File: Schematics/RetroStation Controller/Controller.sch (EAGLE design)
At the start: 10 parts, among them U2 JOYSTICKPTH

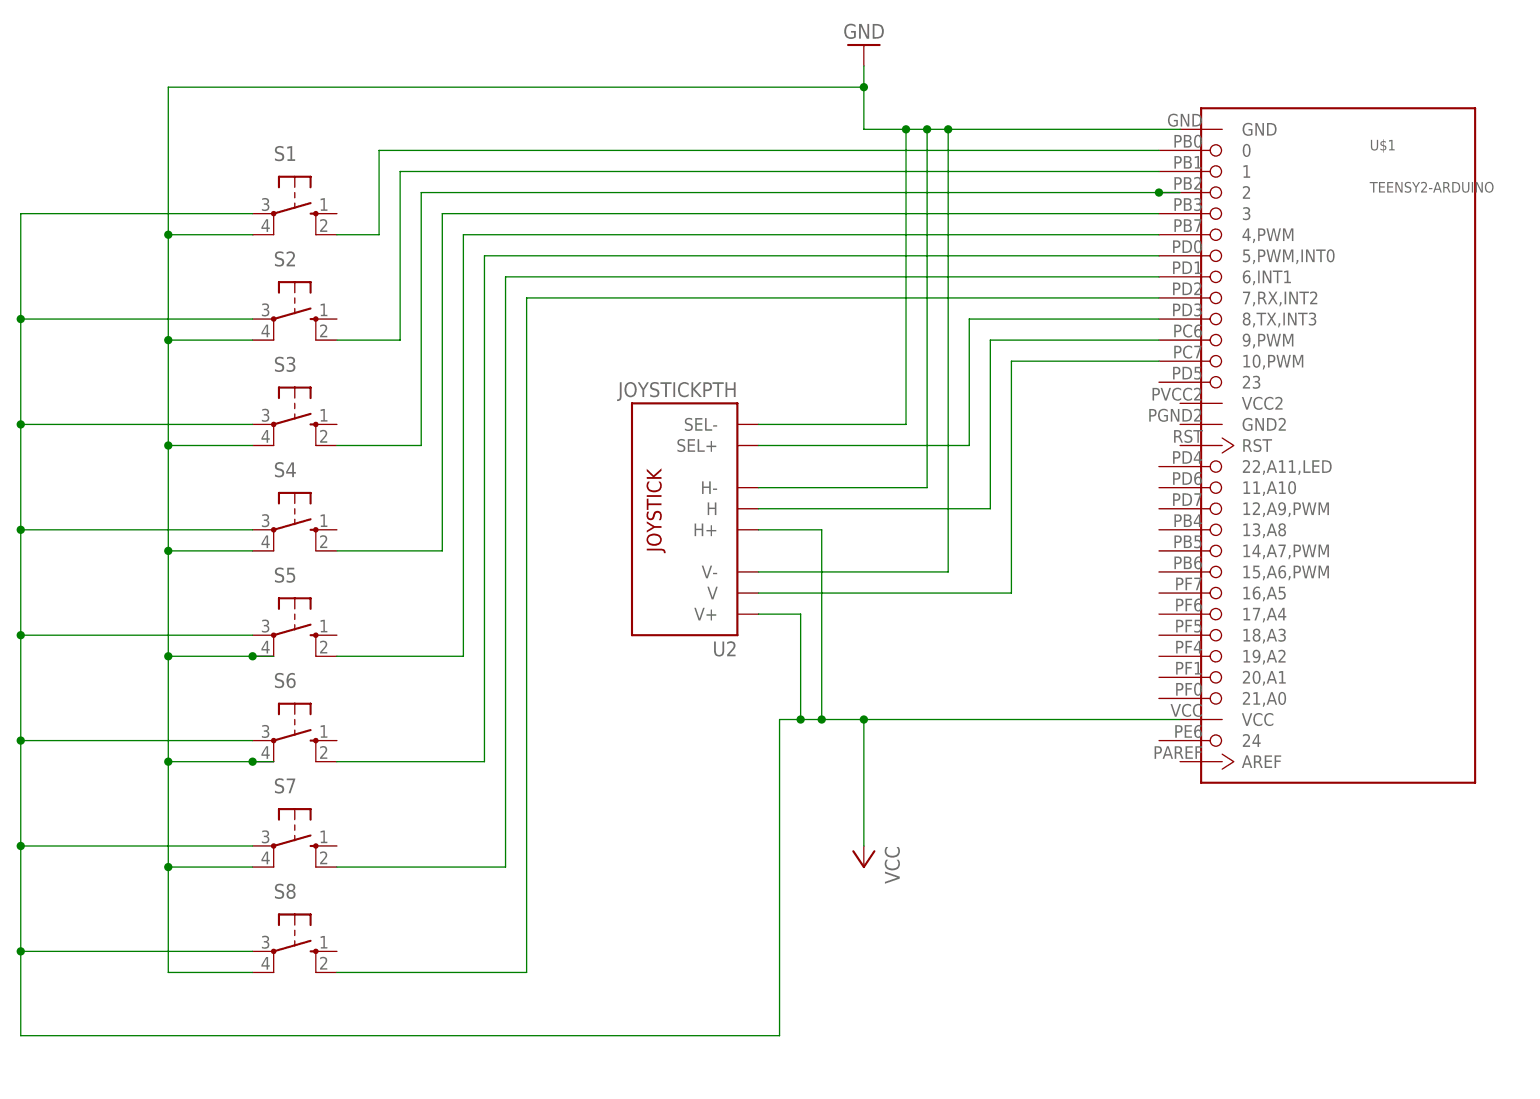
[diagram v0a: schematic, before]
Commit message: Schematics updated to reflect the use of the internal pull-up resistors of the controller's microcontroller Firmware for the internal controller's microcontroller started
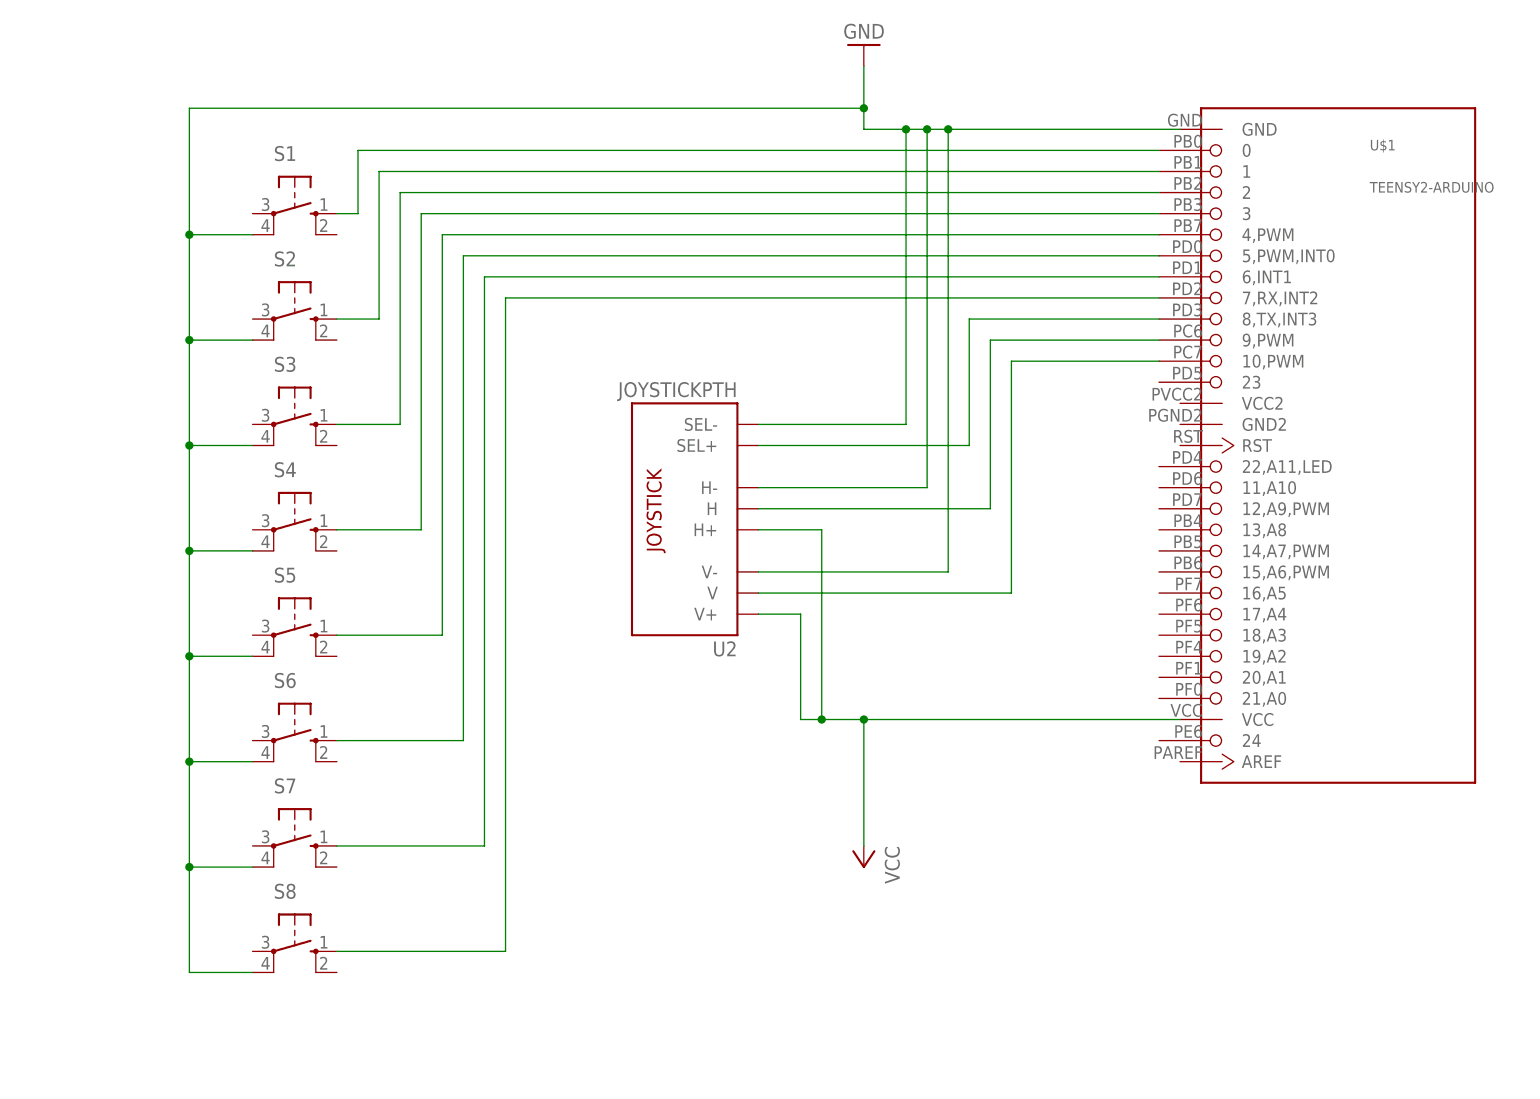
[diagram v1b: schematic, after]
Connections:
- net N$1: now also S1.S; no longer S1.S1
- net N$2: now also S2.S; no longer S2.S1
- net N$3: now also S3.S; no longer S3.S1
- net N$4: now also S4.S; no longer S4.S1
- net N$5: now also S5.S; no longer S5.S1
- net N$6: now also S6.S; no longer S6.S1
- net N$7: now also S7.S; no longer S7.S1
- net N$8: now also S8.S; no longer S8.S1
- net VCC: no longer S1.P, S2.P, S3.P, S4.P, S5.P, S6.P, S7.P, S8.P

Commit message: Created seperate circuits for each button panel.
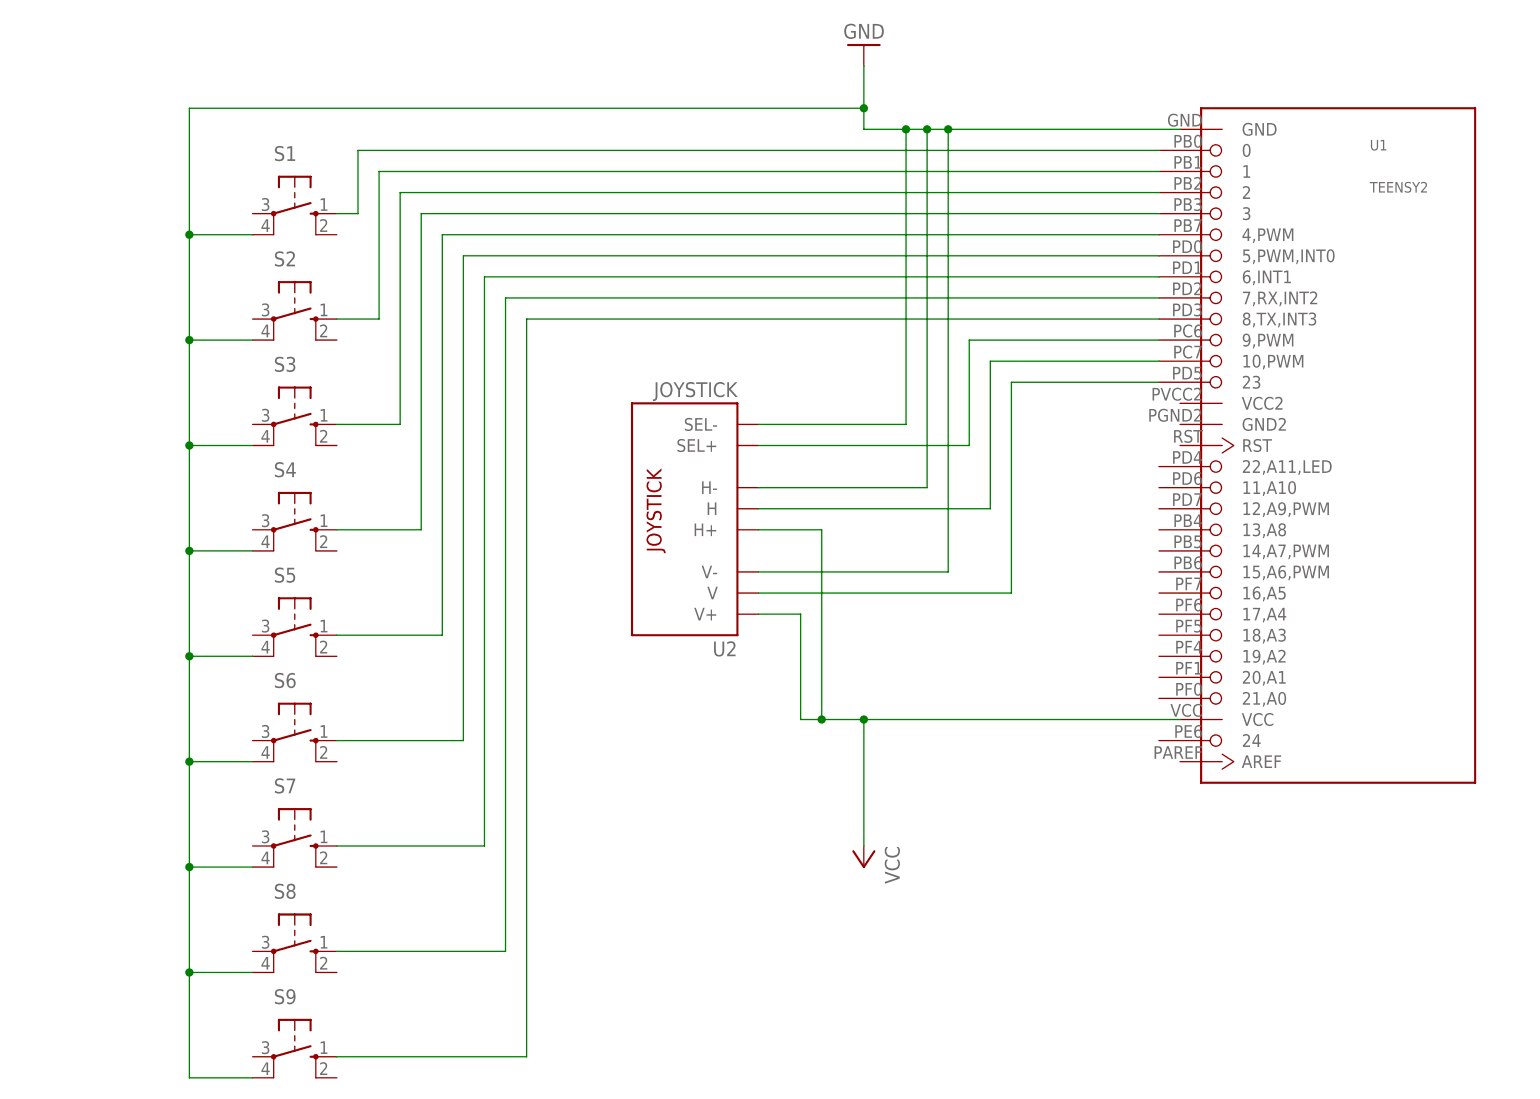
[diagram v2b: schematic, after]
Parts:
- added S9: (no value), switch-omron:10-XX
- U1: value TEENSY2-ARDUINO -> TEENSY2
- U2: value JOYSTICKPTH -> JOYSTICK
- renumbered U$1 to U1
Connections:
- removed net N$13: U1.10,PWM, U2.V
- new net N$10: U1.10,PWM, U2.H
- new net N$9: U1.23, U2.V
- net GND: now also S9.P1
- net N$11: now also U1.9,PWM; no longer U1.8,TX,INT3
- net N$12: now also S9.S, U1.8,TX,INT3; no longer U1.9,PWM, U2.H
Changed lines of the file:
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@@
 </classes>
 <parts>
-<part name="U$1" library="teensy2" deviceset="TEENSY2-ARDUINO" device=""/>
+<part name="U1" library="teensy2" deviceset="TEENSY2-ARDUINO" device="" value="TEENSY2"/>
 <part name="P+1" library="supply1" deviceset="VCC" device=""/>
 <part name="GND" library="supply1" deviceset="GND" device=""/>
@@
 <part name="S7" library="switch-omron" deviceset="10-XX" device=""/>
 <part name="S8" library="switch-omron" deviceset="10-XX" device=""/>
-<part name="U2" library="SparkFun-Electromechanical" deviceset="JOYSTICK" device="PTH"/>
+<part name="U2" library="SparkFun-Electromechanical" deviceset="JOYSTICK" device="PTH" value="JOYSTICK"/>
 <part name="FRAME1" library="frames" deviceset="LETTER_L" device=""/>
+<part name="S9" library="switch-omron" deviceset="10-XX" device=""/>
 </parts>
 <sheets>
@@
 </plain>
 <instances>
-<instance part="U$1" gate="G$1" x="198.12" y="109.22"/>
+<instance part="U1" gate="G$1" x="198.12" y="109.22"/>
 <instance part="P+1" gate="VCC" x="137.16" y="55.88" rot="R180"/>
 <instance part="GND" gate="1" x="137.16" y="154.94" rot="R180"/>
@@
 <instance part="FRAME1" gate="G$1" x="0" y="0"/>
 <instance part="FRAME1" gate="G$2" x="147.32" y="0"/>
+<instance part="S9" gate="1" x="68.58" y="33.02" rot="R270"/>
 </instances>
 <busses>
@@
 <pinref part="P+1" gate="VCC" pin="VCC"/>
 <wire x1="137.16" y1="58.42" x2="137.16" y2="73.66" width="0.1524" layer="91"/>
-<pinref part="U$1" gate="G$1" pin="VCC"/>
+<pinref part="U1" gate="G$1" pin="VCC"/>
 <wire x1="137.16" y1="73.66" x2="175.26" y2="73.66" width="0.1524" layer="91"/>
 <junction x="137.16" y="73.66"/>
@@
 <net name="GND" class="0">
 <segment>
-<pinref part="U$1" gate="G$1" pin="GND"/>
+<pinref part="U1" gate="G$1" pin="GND"/>
 <pinref part="GND" gate="1" pin="GND"/>
 <wire x1="137.16" y1="152.4" x2="137.16" y2="147.32" width="0.1524" layer="91"/>
@@
 <wire x1="55.88" y1="43.18" x2="55.88" y2="55.88" width="0.1524" layer="91"/>
 <junction x="55.88" y="55.88"/>
-</segment>
-</net>
-<net name="N$11" class="0">
-<segment>
-<pinref part="U2" gate="G$1" pin="SEL+"/>
-<wire x1="124.46" y1="106.68" x2="149.86" y2="106.68" width="0.1524" layer="91"/>
-<wire x1="149.86" y1="106.68" x2="149.86" y2="121.92" width="0.1524" layer="91"/>
-<pinref part="U$1" gate="G$1" pin="8,TX,INT3"/>
-<wire x1="149.86" y1="121.92" x2="172.72" y2="121.92" width="0.1524" layer="91"/>
-</segment>
-</net>
-<net name="N$12" class="0">
-<segment>
-<pinref part="U2" gate="G$1" pin="H"/>
-<wire x1="124.46" y1="99.06" x2="152.4" y2="99.06" width="0.1524" layer="91"/>
-<wire x1="152.4" y1="99.06" x2="152.4" y2="119.38" width="0.1524" layer="91"/>
-<pinref part="U$1" gate="G$1" pin="9,PWM"/>
-<wire x1="152.4" y1="119.38" x2="172.72" y2="119.38" width="0.1524" layer="91"/>
-</segment>
-</net>
-<net name="N$13" class="0">
-<segment>
-<pinref part="U2" gate="G$1" pin="V"/>
-<wire x1="124.46" y1="88.9" x2="154.94" y2="88.9" width="0.1524" layer="91"/>
-<wire x1="154.94" y1="88.9" x2="154.94" y2="116.84" width="0.1524" layer="91"/>
-<pinref part="U$1" gate="G$1" pin="10,PWM"/>
-<wire x1="154.94" y1="116.84" x2="172.72" y2="116.84" width="0.1524" layer="91"/>
+<pinref part="S9" gate="1" pin="P1"/>
+<wire x1="63.5" y1="30.48" x2="55.88" y2="30.48" width="0.1524" layer="91"/>
+<wire x1="55.88" y1="30.48" x2="55.88" y2="43.18" width="0.1524" layer="91"/>
+<junction x="55.88" y="43.18"/>
 </segment>
 </net>
@@
 <wire x1="73.66" y1="134.62" x2="76.2" y2="134.62" width="0.1524" layer="91"/>
 <wire x1="76.2" y1="134.62" x2="76.2" y2="142.24" width="0.1524" layer="91"/>
-<pinref part="U$1" gate="G$1" pin="0"/>
+<pinref part="U1" gate="G$1" pin="0"/>
 <wire x1="76.2" y1="142.24" x2="172.72" y2="142.24" width="0.1524" layer="91"/>
 </segment>
@@
 <wire x1="73.66" y1="121.92" x2="78.74" y2="121.92" width="0.1524" layer="91"/>
 <wire x1="78.74" y1="121.92" x2="78.74" y2="139.7" width="0.1524" layer="91"/>
-<pinref part="U$1" gate="G$1" pin="1"/>
+<pinref part="U1" gate="G$1" pin="1"/>
 <wire x1="78.74" y1="139.7" x2="172.72" y2="139.7" width="0.1524" layer="91"/>
 </segment>
@@
 <wire x1="73.66" y1="109.22" x2="81.28" y2="109.22" width="0.1524" layer="91"/>
 <wire x1="81.28" y1="109.22" x2="81.28" y2="137.16" width="0.1524" layer="91"/>
-<pinref part="U$1" gate="G$1" pin="2"/>
+<pinref part="U1" gate="G$1" pin="2"/>
 <wire x1="81.28" y1="137.16" x2="172.72" y2="137.16" width="0.1524" layer="91"/>
 </segment>
@@
 <wire x1="73.66" y1="96.52" x2="83.82" y2="96.52" width="0.1524" layer="91"/>
 <wire x1="83.82" y1="96.52" x2="83.82" y2="134.62" width="0.1524" layer="91"/>
-<pinref part="U$1" gate="G$1" pin="3"/>
+<pinref part="U1" gate="G$1" pin="3"/>
 <wire x1="83.82" y1="134.62" x2="172.72" y2="134.62" width="0.1524" layer="91"/>
 </segment>
@@
 <wire x1="73.66" y1="83.82" x2="86.36" y2="83.82" width="0.1524" layer="91"/>
 <wire x1="86.36" y1="83.82" x2="86.36" y2="132.08" width="0.1524" layer="91"/>
-<pinref part="U$1" gate="G$1" pin="4,PWM"/>
+<pinref part="U1" gate="G$1" pin="4,PWM"/>
 <wire x1="86.36" y1="132.08" x2="172.72" y2="132.08" width="0.1524" layer="91"/>
 </segment>
@@
 <wire x1="73.66" y1="71.12" x2="88.9" y2="71.12" width="0.1524" layer="91"/>
 <wire x1="88.9" y1="71.12" x2="88.9" y2="129.54" width="0.1524" layer="91"/>
-<pinref part="U$1" gate="G$1" pin="5,PWM,INT0"/>
+<pinref part="U1" gate="G$1" pin="5,PWM,INT0"/>
 <wire x1="88.9" y1="129.54" x2="172.72" y2="129.54" width="0.1524" layer="91"/>
 </segment>
@@
 <wire x1="73.66" y1="58.42" x2="91.44" y2="58.42" width="0.1524" layer="91"/>
 <wire x1="91.44" y1="58.42" x2="91.44" y2="127" width="0.1524" layer="91"/>
-<pinref part="U$1" gate="G$1" pin="6,INT1"/>
+<pinref part="U1" gate="G$1" pin="6,INT1"/>
 <wire x1="91.44" y1="127" x2="172.72" y2="127" width="0.1524" layer="91"/>
 </segment>
@@
 <wire x1="73.66" y1="45.72" x2="93.98" y2="45.72" width="0.1524" layer="91"/>
 <wire x1="93.98" y1="45.72" x2="93.98" y2="124.46" width="0.1524" layer="91"/>
-<pinref part="U$1" gate="G$1" pin="7,RX,INT2"/>
+<pinref part="U1" gate="G$1" pin="7,RX,INT2"/>
 <wire x1="93.98" y1="124.46" x2="172.72" y2="124.46" width="0.1524" layer="91"/>
 </segment>
 </net>
+<net name="N$9" class="0">
+<segment>
+<pinref part="U2" gate="G$1" pin="V"/>
+<wire x1="124.46" y1="88.9" x2="154.94" y2="88.9" width="0.1524" layer="91"/>
+<wire x1="154.94" y1="88.9" x2="154.94" y2="114.3" width="0.1524" layer="91"/>
+<pinref part="U1" gate="G$1" pin="23"/>
+<wire x1="154.94" y1="114.3" x2="172.72" y2="114.3" width="0.1524" layer="91"/>
+</segment>
+</net>
+<net name="N$10" class="0">
+<segment>
+<pinref part="U2" gate="G$1" pin="H"/>
+<wire x1="124.46" y1="99.06" x2="152.4" y2="99.06" width="0.1524" layer="91"/>
+<wire x1="152.4" y1="99.06" x2="152.4" y2="116.84" width="0.1524" layer="91"/>
+<pinref part="U1" gate="G$1" pin="10,PWM"/>
+<wire x1="152.4" y1="116.84" x2="172.72" y2="116.84" width="0.1524" layer="91"/>
+</segment>
+</net>
+<net name="N$11" class="0">
+<segment>
+<pinref part="U2" gate="G$1" pin="SEL+"/>
+<wire x1="124.46" y1="106.68" x2="149.86" y2="106.68" width="0.1524" layer="91"/>
+<wire x1="149.86" y1="106.68" x2="149.86" y2="119.38" width="0.1524" layer="91"/>
+<pinref part="U1" gate="G$1" pin="9,PWM"/>
+<wire x1="149.86" y1="119.38" x2="172.72" y2="119.38" width="0.1524" layer="91"/>
+</segment>
+</net>
+<net name="N$12" class="0">
+<segment>
+<pinref part="S9" gate="1" pin="S"/>
+<wire x1="73.66" y1="33.02" x2="96.52" y2="33.02" width="0.1524" layer="91"/>
+<wire x1="96.52" y1="33.02" x2="96.52" y2="121.92" width="0.1524" layer="91"/>
+<pinref part="U1" gate="G$1" pin="8,TX,INT3"/>
+<wire x1="96.52" y1="121.92" x2="172.72" y2="121.92" width="0.1524" layer="91"/>
+</segment>
+</net>
